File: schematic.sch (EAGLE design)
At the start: 51 parts, among them IC1 AD8015, IC2 AD8015

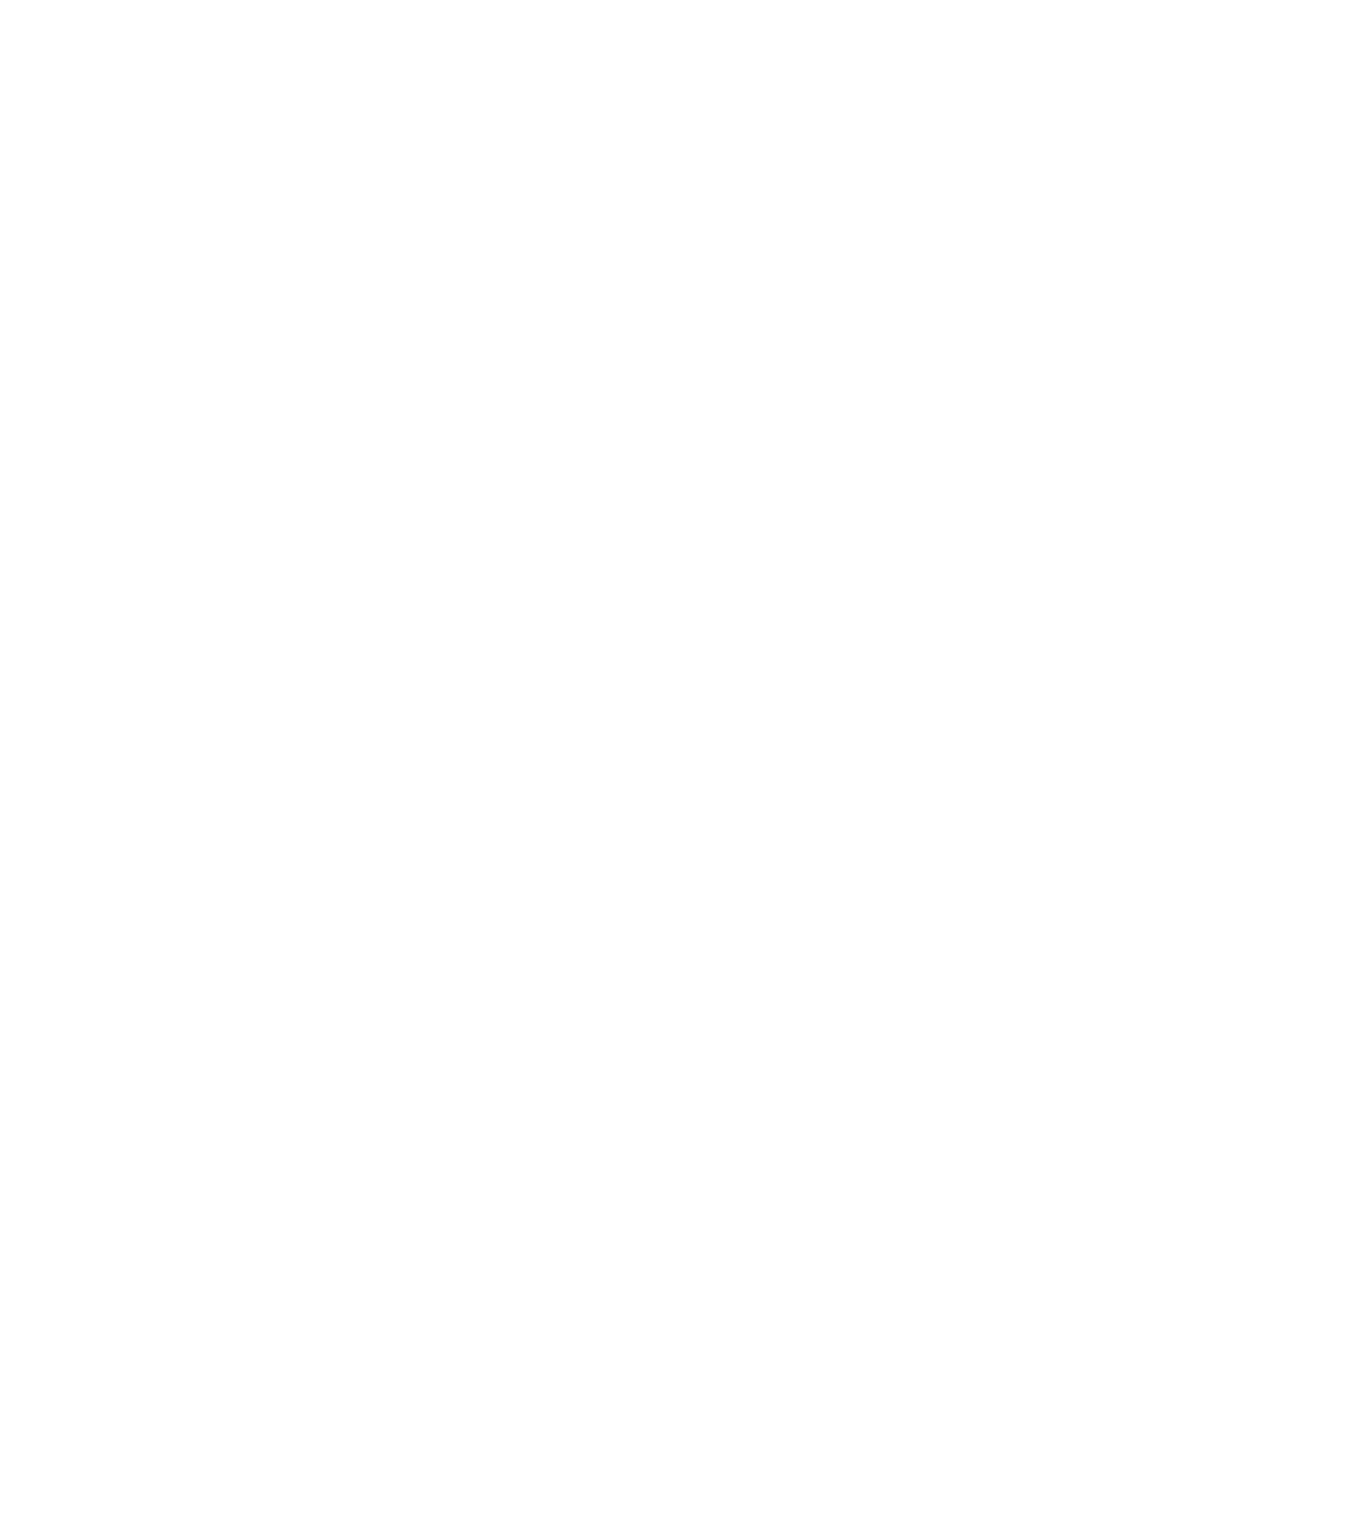
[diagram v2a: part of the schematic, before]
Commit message: Added rest of copies and wired everything together.
Need to add silkscreen and fix photo diodes
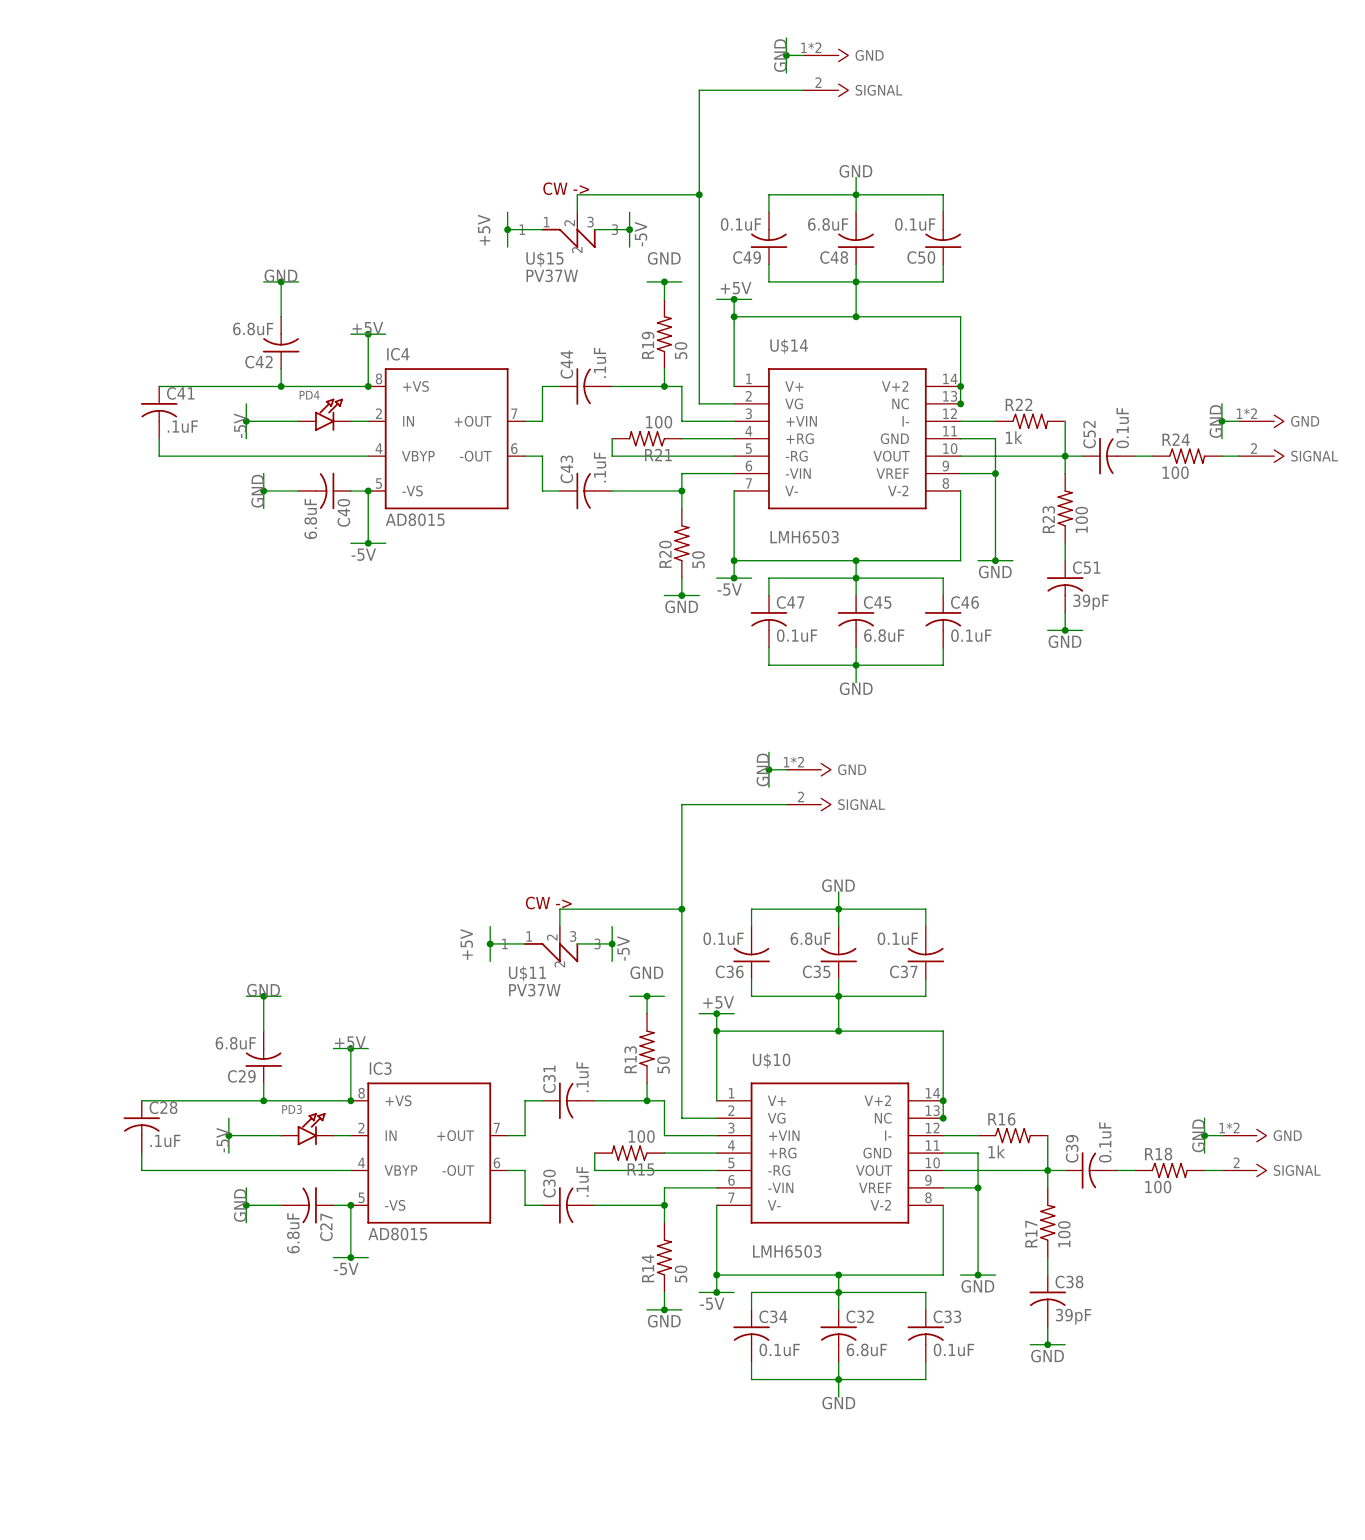
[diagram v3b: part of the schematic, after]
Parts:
- added C27, C29, C32, C35, C40, C42, C45, C48: 6.8uF, rcl:C-USC1206
- added C28, C30, C31, C41, C43, C44: .1uF, rcl:C-USC0603
- added C33, C36, C46, C49: 0.1uF, rcl:C-USC0402
- added C34, C37, C39, C47, C50, C52: 0.1uF, rcl:C-USC0603
- added C38, C51: 39pF, rcl:C-USC0603
- added IC3, IC4: AD8015, analog-devices:AD8015
- added PD3, PD4: (no value), microbuilder:LED1206
- added R13, R14, R19, R20: 50, rcl:R-US_R0603
- added R15, R17, R18, R21, R23, R24: 100, rcl:R-US_R0603
- added R16, R22: 1k, rcl:R-US_R0603
- added U$10, U$14: LMH6503, 12-ChannelEMG:LMH6503
- added U$11, U$15: PV37W, 12-ChannelEMG:PV37W
- added U$12, U$13, U$16, U$17: BNCCONN, 12-ChannelEMG:BNCCONN
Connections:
- new net N$29: C28.2, IC3.VBYP
- new net N$30: IC3.IN, PD3.C
- new net N$31: C31.1, IC3.+OUT
- new net N$32: C30.1, IC3.-OUT
- new net N$33: C30.2, R14.2, U$10.-VIN
- new net N$34: C31.2, R13.1, U$10.+VIN
- new net N$35: R15.1, U$10.+RG
- new net N$36: R15.2, U$10.-RG
- new net N$37: R16.1, U$10.I-
- new net N$38: C39.1, R16.2, R17.2, U$10.VOUT
- new net N$39: C38.1, R17.1
- new net N$40: C39.2, R18.1
- new net N$41: U$10.VG, U$11.2, U$12.SIGNAL
- new net N$42: R18.2, U$13.SIGNAL
- new net N$43: C41.2, IC4.VBYP
- new net N$44: IC4.IN, PD4.C
- new net N$45: C44.1, IC4.+OUT
- new net N$46: C43.1, IC4.-OUT
- new net N$47: C43.2, R20.2, U$14.-VIN
- new net N$48: C44.2, R19.1, U$14.+VIN
- new net N$49: R21.1, U$14.+RG
- new net N$50: R21.2, U$14.-RG
- new net N$51: R22.1, U$14.I-
- new net N$52: C52.1, R22.2, R23.2, U$14.VOUT
- new net N$53: C51.1, R23.1
- new net N$54: C52.2, R24.1
- new net N$55: U$14.VG, U$15.2, U$16.SIGNAL
- new net N$56: R24.2, U$17.SIGNAL
- net +5V: now also C28.1, C29.1, C35.1, C36.1, C37.1, C41.1, C42.1, C48.1, C49.1, C50.1, IC3.+VS, IC4.+VS, U$10.NC, U$10.V+, U$10.V+2, U$11.1, U$14.NC, U$14.V+, U$14.V+2, U$15.1
- net -5V: now also C27.1, C32.1, C33.1, C34.1, C40.1, C45.1, C46.1, C47.1, IC3.-VS, IC4.-VS, PD3.A, PD4.A, U$10.V-, U$10.V-2, U$11.3, U$14.V-, U$14.V-2, U$15.3
- net GND: now also C27.2, C29.2, C32.2, C33.2, C34.2, C35.2, C36.2, C37.2, C38.2, C40.2, C42.2, C45.2, C46.2, C47.2, C48.2, C49.2, C50.2, C51.2, R13.2, R14.1, R19.2, R20.1, U$10.GND, U$10.VREF, U$12.GND, U$13.GND, U$14.GND, U$14.VREF, U$16.GND, U$17.GND

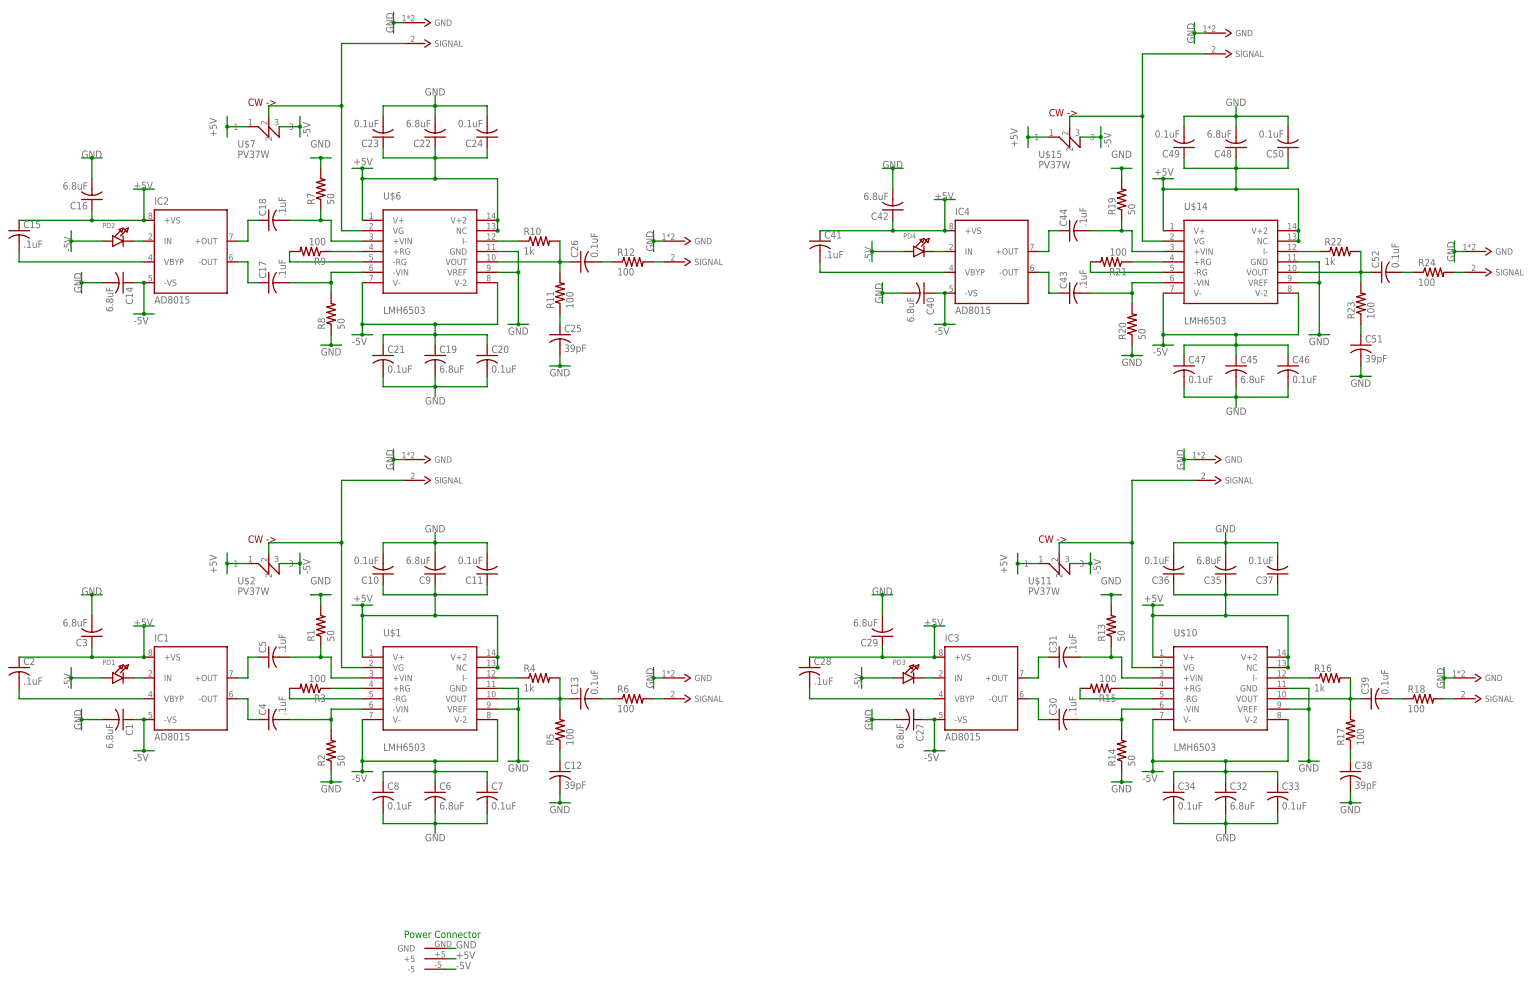
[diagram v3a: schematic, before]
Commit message: Added LMH6624 to end. Major layout rework for high freq AC .
Still has problems. LMH6624 has power inputs on the wrong side of the
chip making it hard to wire to power plane. GND plane is heavily split
in the process of connecting power planes.
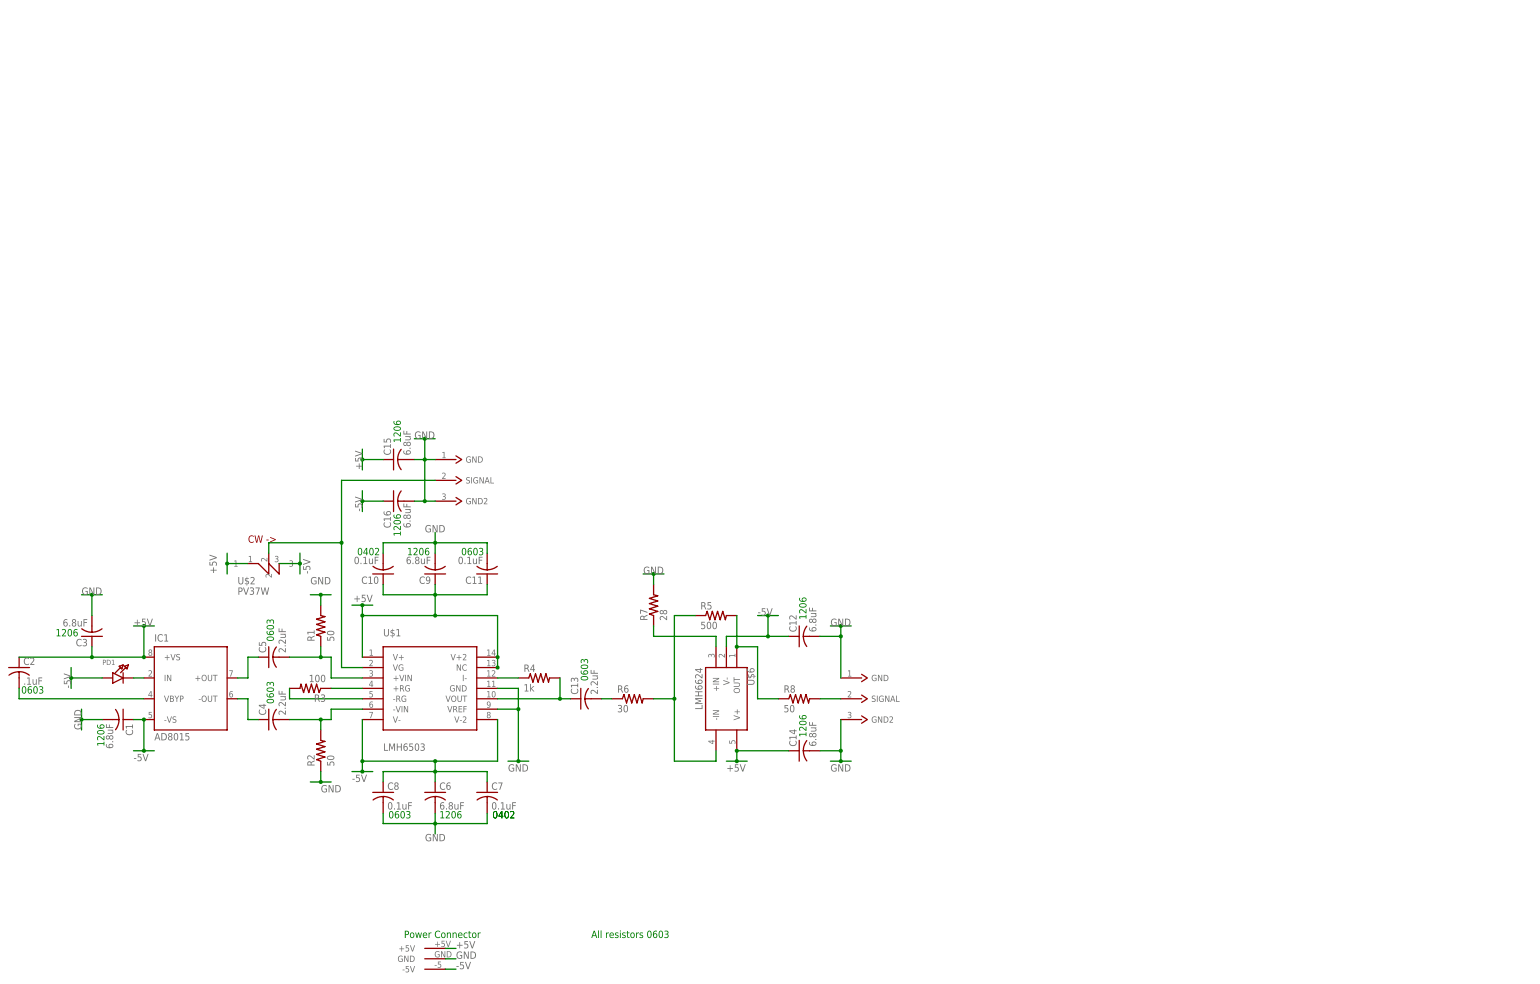
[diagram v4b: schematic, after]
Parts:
- removed C17, C18, C28, C30, C31, C41, C43, C44: .1uF, rcl:C-USC0603
- removed C19, C22, C27, C29, C32, C35, C40, C42, C45, C48: 6.8uF, rcl:C-USC1206
- removed C20, C23, C33, C36, C46, C49: 0.1uF, rcl:C-USC0402
- removed C21, C24, C26, C34, C37, C39, C47, C50, C52: 0.1uF, rcl:C-USC0603
- removed C25, C38, C51: 39pF, rcl:C-USC0603
- removed IC2, IC3, IC4: AD8015, analog-devices:AD8015
- removed PD2, PD3, PD4: (no value), microbuilder:LED1206
- removed R10, R16, R22: 1k, rcl:R-US_R0603
- removed R11, R12, R15, R17, R18, R21, R23, R24, R9: 100, rcl:R-US_R0603
- removed R13, R14, R19, R20: 50, rcl:R-US_R0603
- removed U$10, U$14: LMH6503, 12-ChannelEMG:LMH6503
- removed U$11, U$15, U$7: PV37W, 12-ChannelEMG:PV37W
- removed U$12, U$13, U$16, U$17, U$8, U$9: BNCCONN, 12-ChannelEMG:BNCCONN
- C12: value 39pF -> 6.8uF; device rcl:C-USC0603 -> rcl:C-USC1206
- C13: value 0.1uF -> 2.2uF
- C15: value .1uF -> 6.8uF; device rcl:C-USC0603 -> rcl:C-USC1206
- C4, C5: value .1uF -> 2.2uF
- R5: value 100 -> 500
- R6: value 100 -> 30
- R7: value 50 -> 28
- U$6: value LMH6503 -> LMH6624; device 12-ChannelEMG:LMH6503 -> 12-ChannelEMG:LMH6624
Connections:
- removed net N$17: C18.1, IC2.+OUT
- removed net N$18: C17.1, IC2.-OUT
- removed net N$19: C17.2, R8.2, U$6.-VIN
- removed net N$20: C18.2, R7.1, U$6.+VIN
- removed net N$21: R9.1, U$6.+RG
- removed net N$22: R9.2, U$6.-RG
- removed net N$23: R10.1, U$6.I-
- removed net N$24: C26.1, R10.2, R11.2, U$6.VOUT
- removed net N$25: C25.1, R11.1
- removed net N$26: C26.2, R12.1
- removed net N$27: U$6.VG, U$7.2, U$8.SIGNAL
- removed net N$28: R12.2, U$9.SIGNAL
- removed net N$29: C28.2, IC3.VBYP
- removed net N$30: IC3.IN, PD3.C
- removed net N$31: C31.1, IC3.+OUT
- removed net N$32: C30.1, IC3.-OUT
- removed net N$33: C30.2, R14.2, U$10.-VIN
- removed net N$34: C31.2, R13.1, U$10.+VIN
- removed net N$35: R15.1, U$10.+RG
- removed net N$36: R15.2, U$10.-RG
- removed net N$37: R16.1, U$10.I-
- removed net N$38: C39.1, R16.2, R17.2, U$10.VOUT
- removed net N$39: C38.1, R17.1
- removed net N$40: C39.2, R18.1
- removed net N$41: U$10.VG, U$11.2, U$12.SIGNAL
- removed net N$42: R18.2, U$13.SIGNAL
- removed net N$43: C41.2, IC4.VBYP
- removed net N$44: IC4.IN, PD4.C
- removed net N$45: C44.1, IC4.+OUT
- removed net N$46: C43.1, IC4.-OUT
- removed net N$47: C43.2, R20.2, U$14.-VIN
- removed net N$48: C44.2, R19.1, U$14.+VIN
- removed net N$49: R21.1, U$14.+RG
- removed net N$50: R21.2, U$14.-RG
- removed net N$51: R22.1, U$14.I-
- removed net N$52: C52.1, R22.2, R23.2, U$14.VOUT
- removed net N$53: C51.1, R23.1
- removed net N$54: C52.2, R24.1
- removed net N$55: U$14.VG, U$15.2, U$16.SIGNAL
- removed net N$56: R24.2, U$17.SIGNAL
- net +5V: now also C14.1, U$3.+5V; no longer C16.1, C22.1, C23.1, C24.1, C28.1, C29.1, C35.1, C36.1, C37.1, C41.1, C42.1, C48.1, C49.1, C50.1, IC2.+VS, IC3.+VS, IC4.+VS, U$10.NC, U$10.V+, U$10.V+2, U$11.1, U$14.NC, U$14.V+, U$14.V+2, U$15.1, U$3.+5, U$6.NC, U$6.V+2, U$7.1
- net -5V: now also C12.1, C16.1, U$3.-5V; no longer C14.1, C19.1, C20.1, C21.1, C27.1, C32.1, C33.1, C34.1, C40.1, C45.1, C46.1, C47.1, IC2.-VS, IC3.-VS, IC4.-VS, PD2.A, PD3.A, PD4.A, U$10.V-, U$10.V-2, U$11.3, U$14.V-, U$14.V-2, U$15.3, U$3.-5, U$6.V-2, U$7.3
- net GND: now also C15.2, U$4.GND2, U$5.GND2; no longer C19.2, C20.2, C21.2, C22.2, C23.2, C24.2, C25.2, C27.2, C29.2, C32.2, C33.2, C34.2, C35.2, C36.2, C37.2, C38.2, C40.2, C42.2, C45.2, C46.2, C47.2, C48.2, C49.2, C50.2, C51.2, R13.2, R14.1, R19.2, R20.1, R8.1, U$10.GND, U$10.VREF, U$12.GND, U$13.GND, U$14.GND, U$14.VREF, U$16.GND, U$17.GND, U$6.GND, U$6.VREF, U$8.GND, U$9.GND
- net N$10: no longer R5.2
- net N$11: now also R6.2, U$6.-IN; no longer C12.1
- net N$14: now also R8.2; no longer R6.2
- net N$15: now also R7.1, U$6.+IN; no longer C15.2, IC2.VBYP
- net N$16: now also R5.2, R8.1, U$6.OUT; no longer IC2.IN, PD2.C
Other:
- note added: "0402"
- note added: "0603"
- note added: "1206"
- note added: "All resistors 0603"
- moved on the sheet: C12, C14, C15, C16, R2, R5, R7, R8
